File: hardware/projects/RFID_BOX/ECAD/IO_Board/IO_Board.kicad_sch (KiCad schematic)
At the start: 74 parts, among them J300 J_WAGO_2604-1103, J301 J_WAGO_2604-1103, J302 Conn_01x10_Pin, K300 T92S11D12-24, Q300 2N7002NXAKR, Q301 BSS84AK, Q302 2N7002NXAKR, U300 ISOW7721DFMR, U301 IRM-10-24, U302 MCP39F511A-E/MQ, U306 R-78K5.0-2.0, U307 AP2114H-3.3TRG1

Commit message: IO_Board: Review-Antworten umgesetzt, Sicherungskonzept überarbeitet
Schaltplan:
- Entladekette R305-R310-R321, drei 330k in Reihe parallel zu RV300/C300:
  990 kOhm, C300 unter 60 V in 0,17 s, je Widerstand 77 V effektiv (F1)
- Tiefpass an ISO_EN: R322 1k in Reihe, C329 10nF gegen GND1 (F9)
- FB300 im Abgriff des HV-Teilers entfernt, gegen 1 MOhm wirkungslos (F8)
- F301 von Schurter 0034.3127 auf Bel 5HT 10-R: Keramik sandgefuellt,
  Ausschaltvermoegen 1500 A statt 100 A (F10)
- R323 Sicherungswiderstand 10 Ohm vor F302, begrenzt den Fehlerstrom
  auf 25 A und damit unter die 35 A der MRT (F11)
- R319/R320 als 0R-Bruecken in den UART-Leitungen zu U302

README:
- Abstandsmatrix als Mastertabelle mit L, N, ISO-Insel, SELV, PE und FELD;
  loest die alte Fassung mit NETZ gleicher Pol / Gegenpol ab
- Netzklassen L und N dokumentiert, zugeordnet ueber /PIN_L* und /PIN_N*,
  orthogonal zu den Breitenklassen 230V_ext und 230V_int
- ISO-Insel liegt ueber NT300 auf N-Potential: 0,5 mm gegen N, 3,0 mm gegen L
- Verweis auf den Regelsatz IO_Board.kicad_dru und die U300-Ausnahme
- Bauteiltabellen: Entladekette, R322, R323, F301, Ferritzeile auf FB301/FB302
- FMEA: vier Zeilen fuer F301, F302, Entladekette und Q301 im Linearbetrieb,
  Relaistreiber-Zeile um die Steckerbelegung auf J302 ergaenzt

Datenblaetter: Bel 5HT, Vishay PR01

Co-Authored-By: Claude Opus 5 <noreply@anthropic.com>
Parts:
- removed F301: 10A 250VAC, symbol aa_MyParts:F_0034.3127
- removed FB300: 600R@100MHz, Inductor_SMD:L_0805_2012Metric, symbol aa_MyParts:L_Ferrite_MH2029-601Y
- added C329: 10nF, Capacitor_SMD:C_0603_1608Metric, symbol Device:C
- added F301: 10A 250VAC, symbol aa_MyParts:F_5HT_10-R
- added R305, R310, R321: 330k, Resistor_SMD:R_0805_2012Metric, symbol Device:R
- added R322: 1k, Resistor_SMD:R_0603_1608Metric, symbol Device:R
- added R323: 10R, Resistor_THT:R_Axial_DIN0207_L6.3mm_D2.5mm_P15.24mm_Horizontal, symbol aa_MyParts:R_PR01000101009JA500
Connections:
- net PIN_L_SENSE is gone; now on net PIN_L_FUSED: R303.1
- net GND: now also J302.9 (Pin_9), C329.2; no longer J302.10 (Pin_10), J302.2 (Pin_2)
- net ISO_EN: now also R322.1; no longer R318.1, U300.5 (EN)
- net PIN_L: now also R305.1, R323.1; no longer F302.1
- net PIN_N: now also R321.2
- net relay_en_LS: now also J302.10 (Pin_10); no longer J302.9 (Pin_9)
- new net: C329.1, R318.1, R322.2, U300.5 (EN)
- new net: R310.2, R321.1
- new net: F302.1, R323.2
- new net: R305.2, R310.1
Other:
- moved on the sheet: C300, J300, R318, RV300

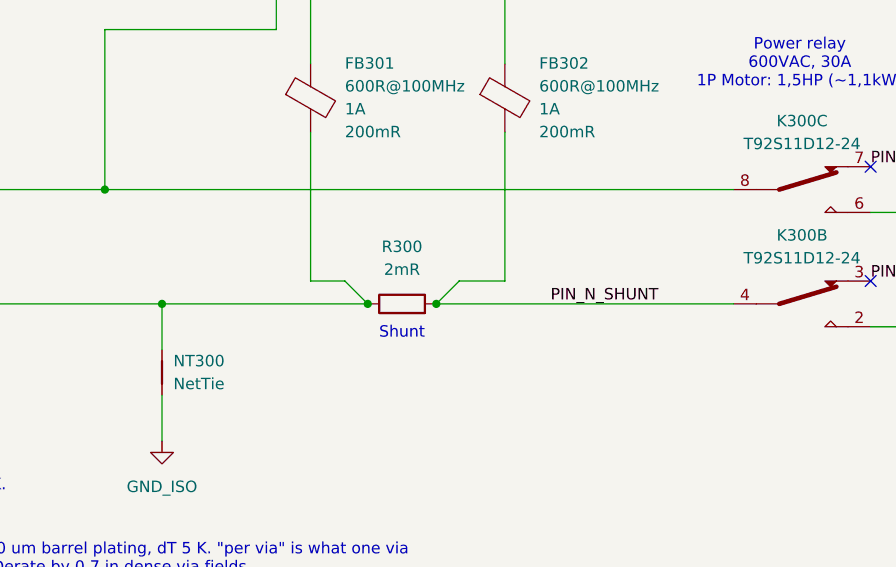
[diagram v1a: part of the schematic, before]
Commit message: IO_Board: Shunt R300 auf pulsfesten CSI2H-2512K-2L00G, Schema V1.2
R300 von CRF2010-FZ-R002ELF auf Bourns CSI2H-2512K-2L00G: 2mOhm +-2%,
+-75ppm/K, 5W @70C, 2512. Sense-Abgriffe liegen wieder auf /PIN_N und
/PIN_N_SHUNT, ERC ohne duplicate_pins, PCB nachgezogen.

README: Shunt-Zeile und Engstellen-Notiz zum Lastpfad aktualisiert,
BOM neu exportiert, Datenblatt abgelegt.

Co-Authored-By: Claude Opus 5 <noreply@anthropic.com>
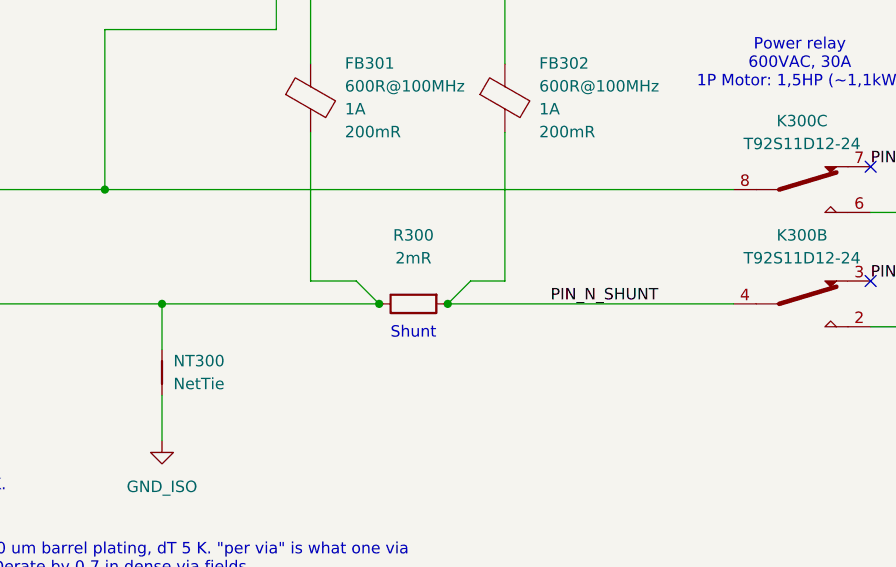
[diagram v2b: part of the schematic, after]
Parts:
- removed R300: 2mR, Resistor_SMD:R_2010_5025Metric, symbol aa_MyParts:R_CRF2010-FZ-R002ELF
- added R300: 2mR, aa_MyParts:R_2512_CSI2H-2512K-2L00G, symbol aa_MyParts:R_CSI2H-2512K-2L00G
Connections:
- net PIN_N: now also R300.2
- net PIN_N_SHUNT: now also R300.1
